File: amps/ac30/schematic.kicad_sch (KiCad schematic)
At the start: 82 parts, among them J1 1/4 in, J2 1/4 in, J3 1/4 in, J4 1/4 in, J5 1/4 in, J6 1/4 in, SW3 SPST, SW4 DPST, T1 4k a-a, T2 280-0-280 V

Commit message: Fix: schematic sheets — real title block, fitted paper, no lettering through circuitry
Every sheet in the corpus shipped with an EMPTY title block ("Title:" and
"Date:" blank, default "Sheet /" furniture) laid onto a fixed A4/A3 page
regardless of the drawing's size, with prose annotations placed by hand
wherever a coordinate looked free when the amp was first drawn. The result
read as an unfinished alpha under a `verified` badge: KiCanvas's default view
is `zoom_to_page()`, so a 150 x 110 mm circuit on an A3 sheet opened as a
postage stamp, and later edits had pushed live circuitry under the prose.

schematic_lib.py — the builder now records each element as a (kind, points,
extra) tuple instead of a finished string, so `write()` can measure and move
what it emits:

- emits a real `(title_block …)` read from the amp's own meta.yaml — Title =
  designation + style, Date = the verification (or added) date, Rev = the
  verification status, Company = Circuit Codex, plus the licence and source
  URL as comments. Fixes all 34 sheets from one place;
- emits `(paper "User" w h)` cut to the drawing, translated to a fixed margin,
  with the bottom 34 mm strip reserved for the worksheet's title block. Sheet
  utilisation of the drawable area went from as low as ~20% to 92-98%;
- `note()` queues prose into a wrapped band under the circuit, and `caption()`
  places a section heading over the block it names, nudging it clear if it
  would print through anything;
- per-symbol default label offsets (the old single default printed every pot's
  value through its own wiper arrow and every transformer's designator through
  its body), plus `place_labels()`, which moves any designator/value block that
  would print over ink;
- transformers and chokes are drawn, not boxed: iron core between two windings,
  centre taps where the part has them, and an optional `spec` lettering slot for
  a ratio or impedance;
- `gnd()` takes a direction, because a flag defaulting to "down" at the HEAD of
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
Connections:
- net MOD-NET g1: no longer V8A.2 (G)
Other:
- note removed: "AC30/6 — Vox AC30/6-style, JMI drawing OS/065 (29-4-60, amended to Issue 4 of 11-9-64) · Circuit Codex · CC-BY-SA 4.0 · redrawn from circuit facts"
- company: (none) -> Circuit Codex
- title: (none) -> AC30 — Vox AC30/6-style

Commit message: Fix: deterministic schematic ids and wires split at every join
- _u() is uuid5 over (amp id, emission order), so a regeneration of an
  unchanged script is byte-identical and a drift gate becomes possible
- write() splits wire segments at symbol pins, wire ends and junction dots,
  so the file connects exactly what the drawing shows under KiCad's
  endpoint-only semantics (270 pins were on a wire's interior; net
  partitions unchanged on all 38 sheets)
- all sheets regenerated; aa864-bassman title block was stale (draft) and
  now matches meta.yaml (verified)

Co-Authored-By: Claude Fable 5.1 <noreply@anthropic.com>
Claude-Session: https://claude.ai/code/session_01KBMfdh37HmCL2iWcBiL5J1
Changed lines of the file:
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@@
   (global_label "GND" (shape input) (at 37.0632 51.9 270)
     (effects (font (size 1.27 1.27)) (justify right)))
-  (wire (pts (xy 65.0632 31.82) (xy 65.0632 43.82))
+  (wire (pts (xy 65.0632 31.82) (xy 65.0632 37.82))
+    (stroke (width 0) (type default)))
+  (wire (pts (xy 65.0632 37.82) (xy 65.0632 43.82))
     (stroke (width 0) (type default)))
   (junction (at 65.0632 37.82) (diameter 0) (color 0 0 0 0))
@@
   (global_label "GND" (shape input) (at 37.0632 87.9 270)
     (effects (font (size 1.27 1.27)) (justify right)))
-  (wire (pts (xy 65.0632 67.82) (xy 65.0632 79.82))
+  (wire (pts (xy 65.0632 67.82) (xy 65.0632 73.82))
+    (stroke (width 0) (type default)))
+  (wire (pts (xy 65.0632 73.82) (xy 65.0632 79.82))
     (stroke (width 0) (type default)))
   (junction (at 65.0632 73.82) (diameter 0) (color 0 0 0 0))
@@
   (wire (pts (xy 83.0632 81.44) (xy 95.0632 81.44))
     (stroke (width 0) (type default)))
-  (wire (pts (xy 95.0632 45.44) (xy 95.0632 93.82))
+  (wire (pts (xy 95.0632 45.44) (xy 95.0632 81.44))
+    (stroke (width 0) (type default)))
+  (wire (pts (xy 95.0632 81.44) (xy 95.0632 93.82))
     (stroke (width 0) (type default)))
   (junction (at 95.0632 81.44) (diameter 0) (color 0 0 0 0))
@@
   (wire (pts (xy 170.873 66.53) (xy 179.063 66.53))
     (stroke (width 0) (type default)))
-  (wire (pts (xy 179.063 30.53) (xy 179.063 66.53))
+  (wire (pts (xy 179.063 30.53) (xy 179.063 49.82))
+    (stroke (width 0) (type default)))
+  (wire (pts (xy 179.063 49.82) (xy 179.063 66.53))
     (stroke (width 0) (type default)))
   (junction (at 179.063 49.82) (diameter 0) (color 0 0 0 0))
@@
     (property "Reference" "R8" (at 186.663 58.43 0) (effects (font (size 1.27 1.27)) (justify left)))
     (property "Value" "1M" (at 186.663 60.83 0) (effects (font (size 1.27 1.27)) (justify left))))
-  (wire (pts (xy 196.063 65.44) (xy 196.063 91.01))
+  (wire (pts (xy 196.063 65.44) (xy 196.063 69.44))
+    (stroke (width 0) (type default)))
+  (wire (pts (xy 196.063 69.44) (xy 196.063 91.01))
     (stroke (width 0) (type default)))
   (symbol (lib_id "cx:R") (at 196.063 94.82 0) (unit 1)
@@
   (wire (pts (xy 207.063 57.44) (xy 207.063 61.82))
     (stroke (width 0) (type default)))
-  (wire (pts (xy 207.063 61.82) (xy 223.063 61.82))
+  (wire (pts (xy 207.063 61.82) (xy 215.063 61.82))
+    (stroke (width 0) (type default)))
+  (wire (pts (xy 215.063 61.82) (xy 223.063 61.82))
     (stroke (width 0) (type default)))
   (wire (pts (xy 207.063 117.44) (xy 207.063 121.82))
@@
   (global_label "GND" (shape input) (at 223.063 77.06 270)
     (effects (font (size 1.27 1.27)) (justify right)))
-  (wire (pts (xy 207.063 38.72) (xy 243.253 38.72))
+  (wire (pts (xy 207.063 38.72) (xy 231.063 38.72))
+    (stroke (width 0) (type default)))
+  (wire (pts (xy 231.063 38.72) (xy 243.253 38.72))
     (stroke (width 0) (type default)))
   (junction (at 207.063 38.72) (diameter 0) (color 0 0 0 0))
   (junction (at 231.063 38.72) (diameter 0) (color 0 0 0 0))
-  (wire (pts (xy 207.063 98.72) (xy 243.253 98.72))
+  (wire (pts (xy 207.063 98.72) (xy 231.063 98.72))
+    (stroke (width 0) (type default)))
+  (wire (pts (xy 231.063 98.72) (xy 243.253 98.72))
     (stroke (width 0) (type default)))
   (junction (at 207.063 98.72) (diameter 0) (color 0 0 0 0))
@@
     (property "Reference" "VR3" (at 235.265 81.99 0) (effects (font (size 1.27 1.27)) (justify left)))
     (property "Value" "250k cut" (at 235.265 84.39 0) (effects (font (size 1.27 1.27)) (justify left))))
-  (wire (pts (xy 231.063 87.44) (xy 231.063 98.72))
+  (wire (pts (xy 231.063 87.44) (xy 231.063 91.82))
+    (stroke (width 0) (type default)))
+  (wire (pts (xy 231.063 91.82) (xy 231.063 98.72))
     (stroke (width 0) (type default)))
   (wire (pts (xy 236.143 83.63) (xy 236.143 91.82))
@@
   (wire (pts (xy 250.873 38.72) (xy 259.063 38.72))
     (stroke (width 0) (type default)))
-  (wire (pts (xy 259.063 35.82) (xy 259.063 77.44))
+  (wire (pts (xy 259.063 35.82) (xy 259.063 38.72))
+    (stroke (width 0) (type default)))
+  (wire (pts (xy 259.063 38.72) (xy 259.063 71.82))
+    (stroke (width 0) (type default)))
+  (wire (pts (xy 259.063 71.82) (xy 259.063 77.44))
     (stroke (width 0) (type default)))
   (junction (at 259.063 38.72) (diameter 0) (color 0 0 0 0))
@@
   (wire (pts (xy 250.873 98.72) (xy 263.063 98.72))
     (stroke (width 0) (type default)))
-  (wire (pts (xy 263.063 98.72) (xy 263.063 149.44))
+  (wire (pts (xy 263.063 98.72) (xy 263.063 107.82))
+    (stroke (width 0) (type default)))
+  (wire (pts (xy 263.063 107.82) (xy 263.063 143.82))
+    (stroke (width 0) (type default)))
+  (wire (pts (xy 263.063 143.82) (xy 263.063 149.44))
     (stroke (width 0) (type default)))
   (junction (at 263.063 107.82) (diameter 0) (color 0 0 0 0))
@@
   (wire (pts (xy 289.063 150.805) (xy 329.063 150.805))
     (stroke (width 0) (type default)))
-  (wire (pts (xy 329.063 42.805) (xy 329.063 159.82))
+  (wire (pts (xy 329.063 42.805) (xy 329.063 78.805))
+    (stroke (width 0) (type default)))
+  (wire (pts (xy 329.063 78.805) (xy 329.063 114.805))
+    (stroke (width 0) (type default)))
+  (wire (pts (xy 329.063 114.805) (xy 329.063 150.805))
+    (stroke (width 0) (type default)))
+  (wire (pts (xy 329.063 150.805) (xy 329.063 159.82))
     (stroke (width 0) (type default)))
   (junction (at 329.063 78.805) (diameter 0) (color 0 0 0 0))
@@
     (stroke (width 0) (type default)))
   (junction (at 337.063 57.82) (diameter 0) (color 0 0 0 0))
-  (wire (pts (xy 337.063 21.82) (xy 337.063 89.74))
+  (wire (pts (xy 337.063 21.82) (xy 337.063 57.82))
+    (stroke (width 0) (type default)))
+  (wire (pts (xy 337.063 57.82) (xy 337.063 89.74))
     (stroke (width 0) (type default)))
   (wire (pts (xy 337.063 89.74) (xy 350.173 89.74))
@@
   (wire (pts (xy 367.953 92.28) (xy 381.983 92.28))
     (stroke (width 0) (type default)))
-  (wire (pts (xy 367.953 97.36) (xy 381.983 97.36))
+  (wire (pts (xy 367.953 97.36) (xy 375.063 97.36))
+    (stroke (width 0) (type default)))
+  (wire (pts (xy 375.063 97.36) (xy 381.983 97.36))
     (stroke (width 0) (type default)))
   (symbol (lib_id "cx:JACK") (at 387.063 94.82 0) (unit 1)
@@
     (property "Reference" "R40" (at 39.8632 161.82 270) (effects (font (size 1.27 1.27)) (justify left)))
     (property "Value" "15k" (at 39.8632 164.22 270) (effects (font (size 1.27 1.27)) (justify left))))
-  (wire (pts (xy 46.8732 167.82) (xy 67.0632 167.82))
+  (wire (pts (xy 46.8732 167.82) (xy 57.0632 167.82))
+    (stroke (width 0) (type default)))
+  (wire (pts (xy 57.0632 167.82) (xy 67.0632 167.82))
     (stroke (width 0) (type default)))
   (junction (at 57.0632 167.82) (diameter 0) (color 0 0 0 0))
@@
   (wire (pts (xy 51.0632 259.82) (xy 51.0632 251.82))
     (stroke (width 0) (type default)))
-  (wire (pts (xy 42.8732 251.82) (xy 63.0632 251.82))
+  (wire (pts (xy 42.8732 251.82) (xy 51.0632 251.82))
+    (stroke (width 0) (type default)))
+  (wire (pts (xy 51.0632 251.82) (xy 63.0632 251.82))
     (stroke (width 0) (type default)))
   (junction (at 51.0632 251.82) (diameter 0) (color 0 0 0 0))
@@
   (wire (pts (xy 339.063 226.44) (xy 339.063 231.82))
     (stroke (width 0) (type default)))
-  (wire (pts (xy 321.063 231.82) (xy 357.443 231.82))
+  (wire (pts (xy 321.063 231.82) (xy 339.063 231.82))
+    (stroke (width 0) (type default)))
+  (wire (pts (xy 339.063 231.82) (xy 349.063 231.82))
+    (stroke (width 0) (type default)))
+  (wire (pts (xy 349.063 231.82) (xy 357.443 231.82))
     (stroke (width 0) (type default)))
   (junction (at 339.063 231.82) (diameter 0) (color 0 0 0 0))
@@
   (wire (pts (xy 309.063 261.82) (xy 315.253 261.82))
     (stroke (width 0) (type default)))
-  (wire (pts (xy 322.873 261.82) (xy 337.063 261.82))
+  (wire (pts (xy 322.873 261.82) (xy 325.063 261.82))
+    (stroke (width 0) (type default)))
+  (wire (pts (xy 325.063 261.82) (xy 337.063 261.82))
     (stroke (width 0) (type default)))
   (junction (at 325.063 261.82) (diameter 0) (color 0 0 0 0))
@@
   (wire (pts (xy 377.063 261.82) (xy 383.253 261.82))
     (stroke (width 0) (type default)))
-  (wire (pts (xy 390.873 261.82) (xy 405.063 261.82))
+  (wire (pts (xy 390.873 261.82) (xy 393.063 261.82))
+    (stroke (width 0) (type default)))
+  (wire (pts (xy 393.063 261.82) (xy 405.063 261.82))
     (stroke (width 0) (type default)))
   (junction (at 393.063 261.82) (diameter 0) (color 0 0 0 0))

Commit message: Fix: schematic wiring on m1987, aa864-bassman, ac30, m1959, ga40, aa1164, aa964
- 58 open pins closed: leads that stopped short of their flags, pins
  missed by 0.01-0.11 mm, snubbers and bright caps with no leads
- two shorts the isolated-pin check cannot see: aa864-bassman V6 anode
  lead ran through its grounded cathode (plate rail to chassis) and its V5
  coupler drop shorted RGL1; m1987 RB1/RB2 stood on the wire they bridge
- 14 dated waivers: m1959 C29-C31 (factory sheet prints them unconnected),
  ga40 V2/V3/VR3.3 (net_map excluded tubes, free rheostat lug)
- all seven sheets pass connectivity and verify_schematic_nets

Co-Authored-By: Claude Fable 5.1 <noreply@anthropic.com>
Claude-Session: https://claude.ai/code/session_01KBMfdh37HmCL2iWcBiL5J1
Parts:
- removed QS: 3-pin, symbol cx:JACK
- added F1: 3A, symbol cx:FUSE
- QS: renamed from F1; value 3A -> 3-pin; symbol cx:FUSE -> cx:JACK
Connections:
- net at R25.1: now also V3.3 (G2)
- net at R26.1: now also V4.3 (G2)
- net at T2.2 (PRI_2): now also QS.2 (S)
- net at QS.1 (T): now also F1.1
- net at SW4.1: now also F1.2; no longer QS.2
- net at V6.1 (P): now also T1.3 (PRI_B), V4.1 (P)
- net at V6.3 (G2): now also R30.1
- net at V5.3 (G2): now also R29.1
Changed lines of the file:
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@@
   (wire (pts (xy 272.873 35.82) (xy 281.443 35.82))
-    (stroke (width 0) (type default)))
-  (wire (pts (xy 296.683 34.55) (xy 299.063 34.55))
     (stroke (width 0) (type default)))
   (symbol (lib_id "cx:R") (at 305.063 34.55 90) (unit 1)
@@
     (property "Reference" "R25" (at 301.863 28.55 270) (effects (font (size 1.27 1.27)) (justify left)))
     (property "Value" "100" (at 301.863 30.95 270) (effects (font (size 1.27 1.27)) (justify left))))
+  (wire (pts (xy 296.683 34.55) (xy 301.253 34.55))
+    (stroke (width 0) (type default)))
   (wire (pts (xy 308.873 34.55) (xy 313.063 34.55))
     (stroke (width 0) (type default)))
@@
   (wire (pts (xy 272.873 71.82) (xy 281.443 71.82))
     (stroke (width 0) (type default)))
-  (wire (pts (xy 296.683 70.55) (xy 299.063 70.55))
-    (stroke (width 0) (type default)))
   (symbol (lib_id "cx:R") (at 305.063 70.55 90) (unit 1)
     (in_bom yes) (on_board yes)
     (property "Reference" "R29" (at 301.863 64.55 270) (effects (font (size 1.27 1.27)) (justify left)))
     (property "Value" "100" (at 301.863 66.95 270) (effects (font (size 1.27 1.27)) (justify left))))
+  (wire (pts (xy 296.683 70.55) (xy 301.253 70.55))
+    (stroke (width 0) (type default)))
   (wire (pts (xy 308.873 70.55) (xy 313.063 70.55))
     (stroke (width 0) (type default)))
@@
   (wire (pts (xy 276.873 107.82) (xy 281.443 107.82))
     (stroke (width 0) (type default)))
-  (wire (pts (xy 296.683 106.55) (xy 299.063 106.55))
-    (stroke (width 0) (type default)))
   (symbol (lib_id "cx:R") (at 305.063 106.55 90) (unit 1)
     (in_bom yes) (on_board yes)
     (property "Reference" "R26" (at 301.863 100.55 270) (effects (font (size 1.27 1.27)) (justify left)))
     (property "Value" "100" (at 301.863 102.95 270) (effects (font (size 1.27 1.27)) (justify left))))
+  (wire (pts (xy 296.683 106.55) (xy 301.253 106.55))
+    (stroke (width 0) (type default)))
   (wire (pts (xy 308.873 106.55) (xy 313.063 106.55))
     (stroke (width 0) (type default)))
@@
   (wire (pts (xy 276.873 143.82) (xy 281.443 143.82))
     (stroke (width 0) (type default)))
-  (wire (pts (xy 296.683 142.55) (xy 299.063 142.55))
-    (stroke (width 0) (type default)))
   (symbol (lib_id "cx:R") (at 305.063 142.55 90) (unit 1)
     (in_bom yes) (on_board yes)
     (property "Reference" "R30" (at 301.863 136.55 270) (effects (font (size 1.27 1.27)) (justify left)))
     (property "Value" "100" (at 301.863 138.95 270) (effects (font (size 1.27 1.27)) (justify left))))
+  (wire (pts (xy 296.683 142.55) (xy 301.253 142.55))
+    (stroke (width 0) (type default)))
   (wire (pts (xy 308.873 142.55) (xy 313.063 142.55))
     (stroke (width 0) (type default)))
@@
   (wire (pts (xy 289.063 129.82) (xy 343.063 129.82))
     (stroke (width 0) (type default)))
-  (junction (at 343.063 129.82) (diameter 0) (color 0 0 0 0))
   (wire (pts (xy 343.063 93.82) (xy 343.063 99.9))
     (stroke (width 0) (type default)))
+  (wire (pts (xy 343.063 99.9) (xy 343.063 129.82))
+    (stroke (width 0) (type default)))
+  (junction (at 343.063 99.9) (diameter 0) (color 0 0 0 0))
   (wire (pts (xy 343.063 99.9) (xy 350.173 99.9))
     (stroke (width 0) (type default)))
@@
   (global_label "GND" (shape input) (at 375.063 105.82 270)
     (effects (font (size 1.27 1.27)) (justify right)))
-  (text "4 kOhm anode to anode; 8 and 15 Ohm secondary taps" (at 337.063 117.82 0)
+  (text "4 kOhm anode to anode; 8 and 15 Ohm secondary taps" (at 347.063 137.82 0)
     (effects (font (size 1.15 1.15)) (justify left)))
   (text "Vibrato/Tremolo channel — ‘Vibravox’" (at 23.0632 121.82 0)

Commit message: Add: real tube pin numbers and readable valve glyphs on every schematic
Phase B of the drawing program. A factory service sheet numbers every tube
pin, because the number is what a technician puts a probe on. This corpus
printed none, and the numbers hidden in its symbols were positional
placeholders (P=1, G=2, K=3) that would have published a 6V6GT's plate as
pin 1 when it is pin 3.

1055 electrodes now carry the real number, 1027 lettered (27 are shared
filaments deduped, 1 dropped for want of clear space on the 6G2). Resolved per
instance from reference/tubes/<slug>.yaml through the same alias resolution the
layout renderer uses, so a 12AX7 section and a 6SL7 section each get their own
basing. A valve whose basing the corpus does not carry prints nothing rather
than a wrong number.

Section letters and basing units are now separate things, which cost a detour
worth recording. The RCA 12AX7-A sheet reads "Pin 1 - Plate of Unit No.2 ...
Pin 6 - Plate of Unit No.1", so unit numbering is not pin order; the 5Y3 and
GZ34 number their units in opposite pin order, so nothing positional can
express it. But the section LETTER is a designator, not a basing fact: this
corpus, like every technician, calls the first stage in signal order V1A, and
five amps' prose already did. On four amps the factory sheets put that first
stage on the other half -- the AA764's own schematic prints +200 V on pin 1 --
so those drawings now state their unit explicitly, each citing its source, and
no letter, netlist, parts list or layout comment changed. 183 layout comments
agree with the printed numbers, 0 disagree. A guard fires if two halves of one
bottle resolve to the same unit, which is exactly how this was found.

Glyphs: the cathode gains a bracket and filament hairpin so it can no longer be
confused with the plate bar, the pentode's screen sits on its own row, and a
rectifier draws as one envelope over its sections instead of two apparent
bottles. Line weights are scaled per sheet to a co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
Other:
- note added: "1"
- note added: "2"
- note added: "3"
- note added: "4"
- note added: "6"
- note added: "7"
- note added: "8"
- note added: "9"

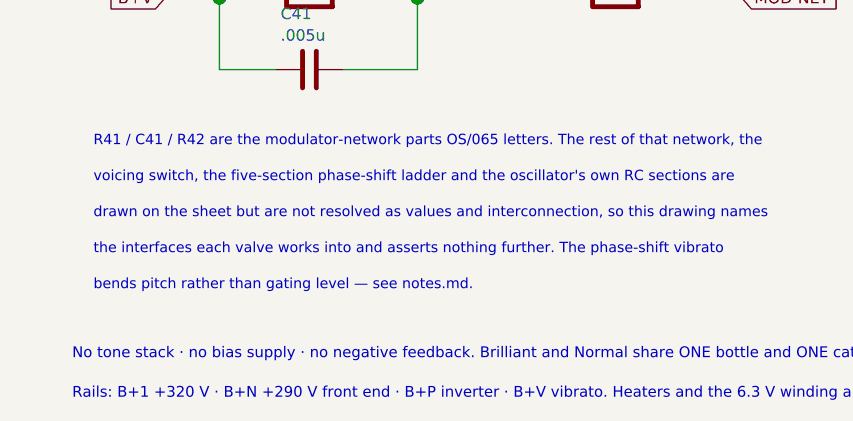
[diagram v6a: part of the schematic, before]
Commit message: Fix: schematic sheet notes no longer name repository files
Thirty-seven committed sheets rendered footnotes and section notes such as
"Heaters and PT primary omitted — see netlist.cir and meta.yaml" or
"excluded from netlist.cir (notes.md)" to visitors through KiCanvas. The
prose sweeps never counted sheets. Rewritten in the site's own words — the
netlist, the sources list, the circuit story, the parts list, the board
drawing — in 59 strings across 33 draw scripts, keeping every technical
claim as it was; the three tone sheets (6G4, 6G5, 6G6-B) are under repair
elsewhere and keep theirs for now. The sweep touched only strings passed to
the sheet's note, text, caption and footnote calls, never a path or a value.

Gates: check_schematics 40/0, connectivity 0 isolated pins;
verify_schematic_nets 40 clean; only the regenerated sheets and their served
copies changed.

Co-Authored-By: Claude Fable 5.1 <noreply@anthropic.com>
Claude-Session: https://claude.ai/code/session_01KBMfdh37HmCL2iWcBiL5J1
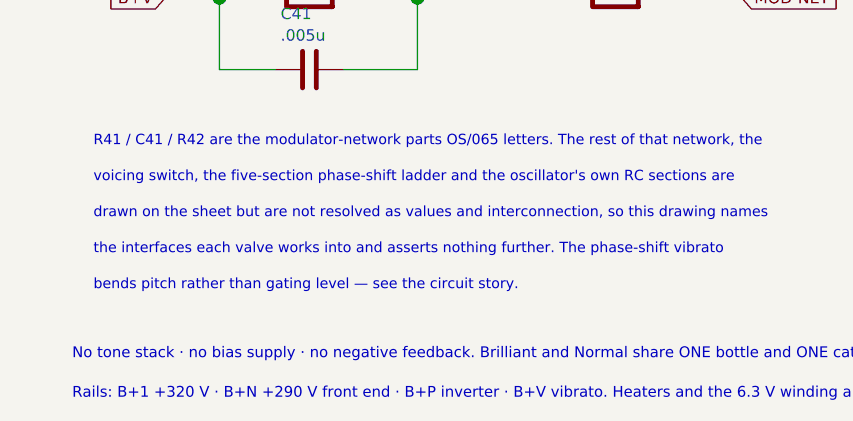
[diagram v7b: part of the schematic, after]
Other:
- note added: "bends pitch rather than gating level — see the circuit story."
- note removed: "bends pitch rather than gating level — see notes.md."
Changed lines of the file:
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@@
   (text "the interfaces each valve works into and asserts nothing further. The phase-shift vibrato" (at 15.0632 279.82 0)
     (effects (font (size 1.15 1.15)) (justify left)))
-  (text "bends pitch rather than gating level — see notes.md." (at 15.0632 283.82 0)
+  (text "bends pitch rather than gating level — see the circuit story." (at 15.0632 283.82 0)
     (effects (font (size 1.15 1.15)) (justify left)))
   (text "Power — Haddon mains transformer (280-0-280 V, 160 mA HT), GZ34 rectifier, 10-20 H Radiospares choke" (at 207.063 191.82 0)
